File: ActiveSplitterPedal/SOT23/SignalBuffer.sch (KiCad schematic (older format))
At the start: 11 parts, among them SW1 SW_SPDT, U1 OPA842, U5 DG468DV_T1_E3

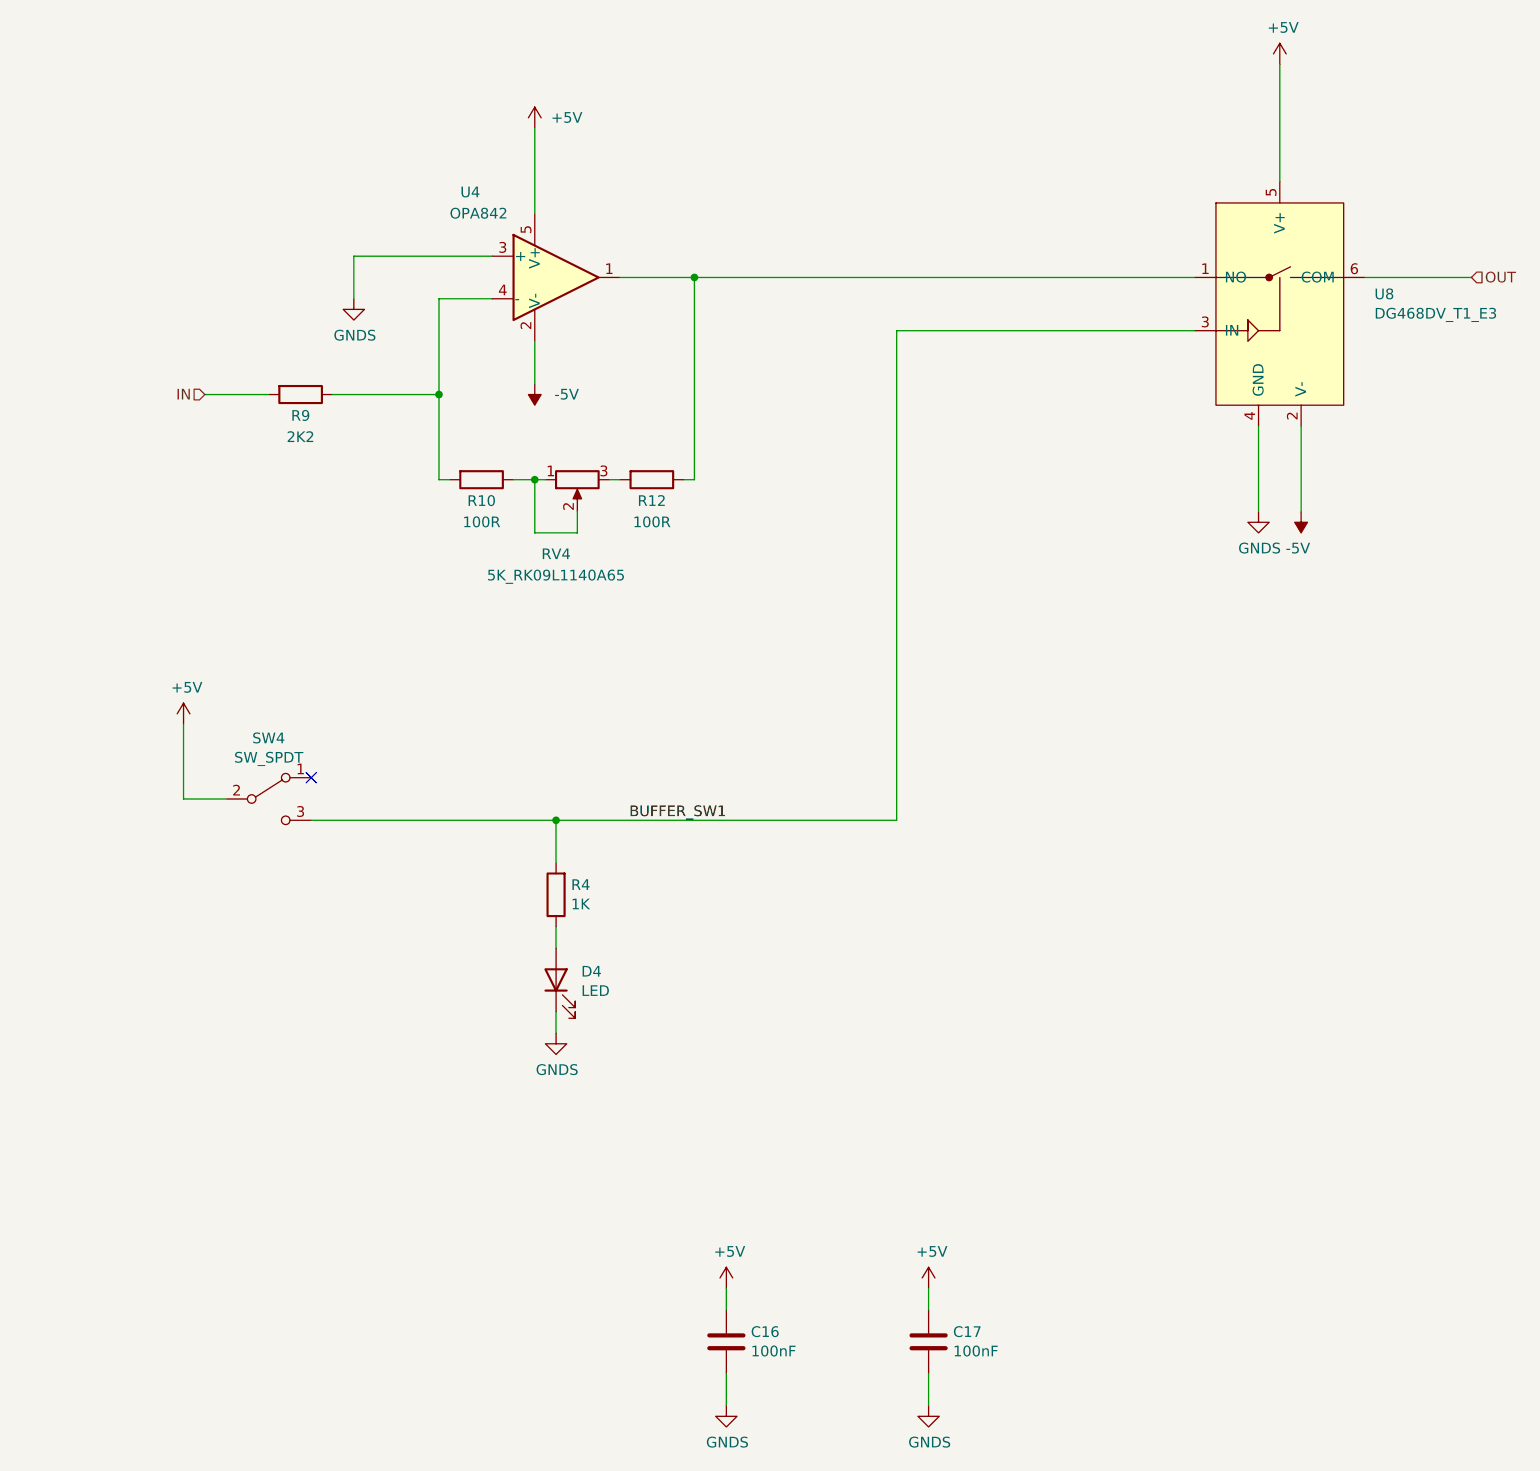
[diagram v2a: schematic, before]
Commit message: upgraded opamp from OPA842 to OPA197 (better performance/lower price)
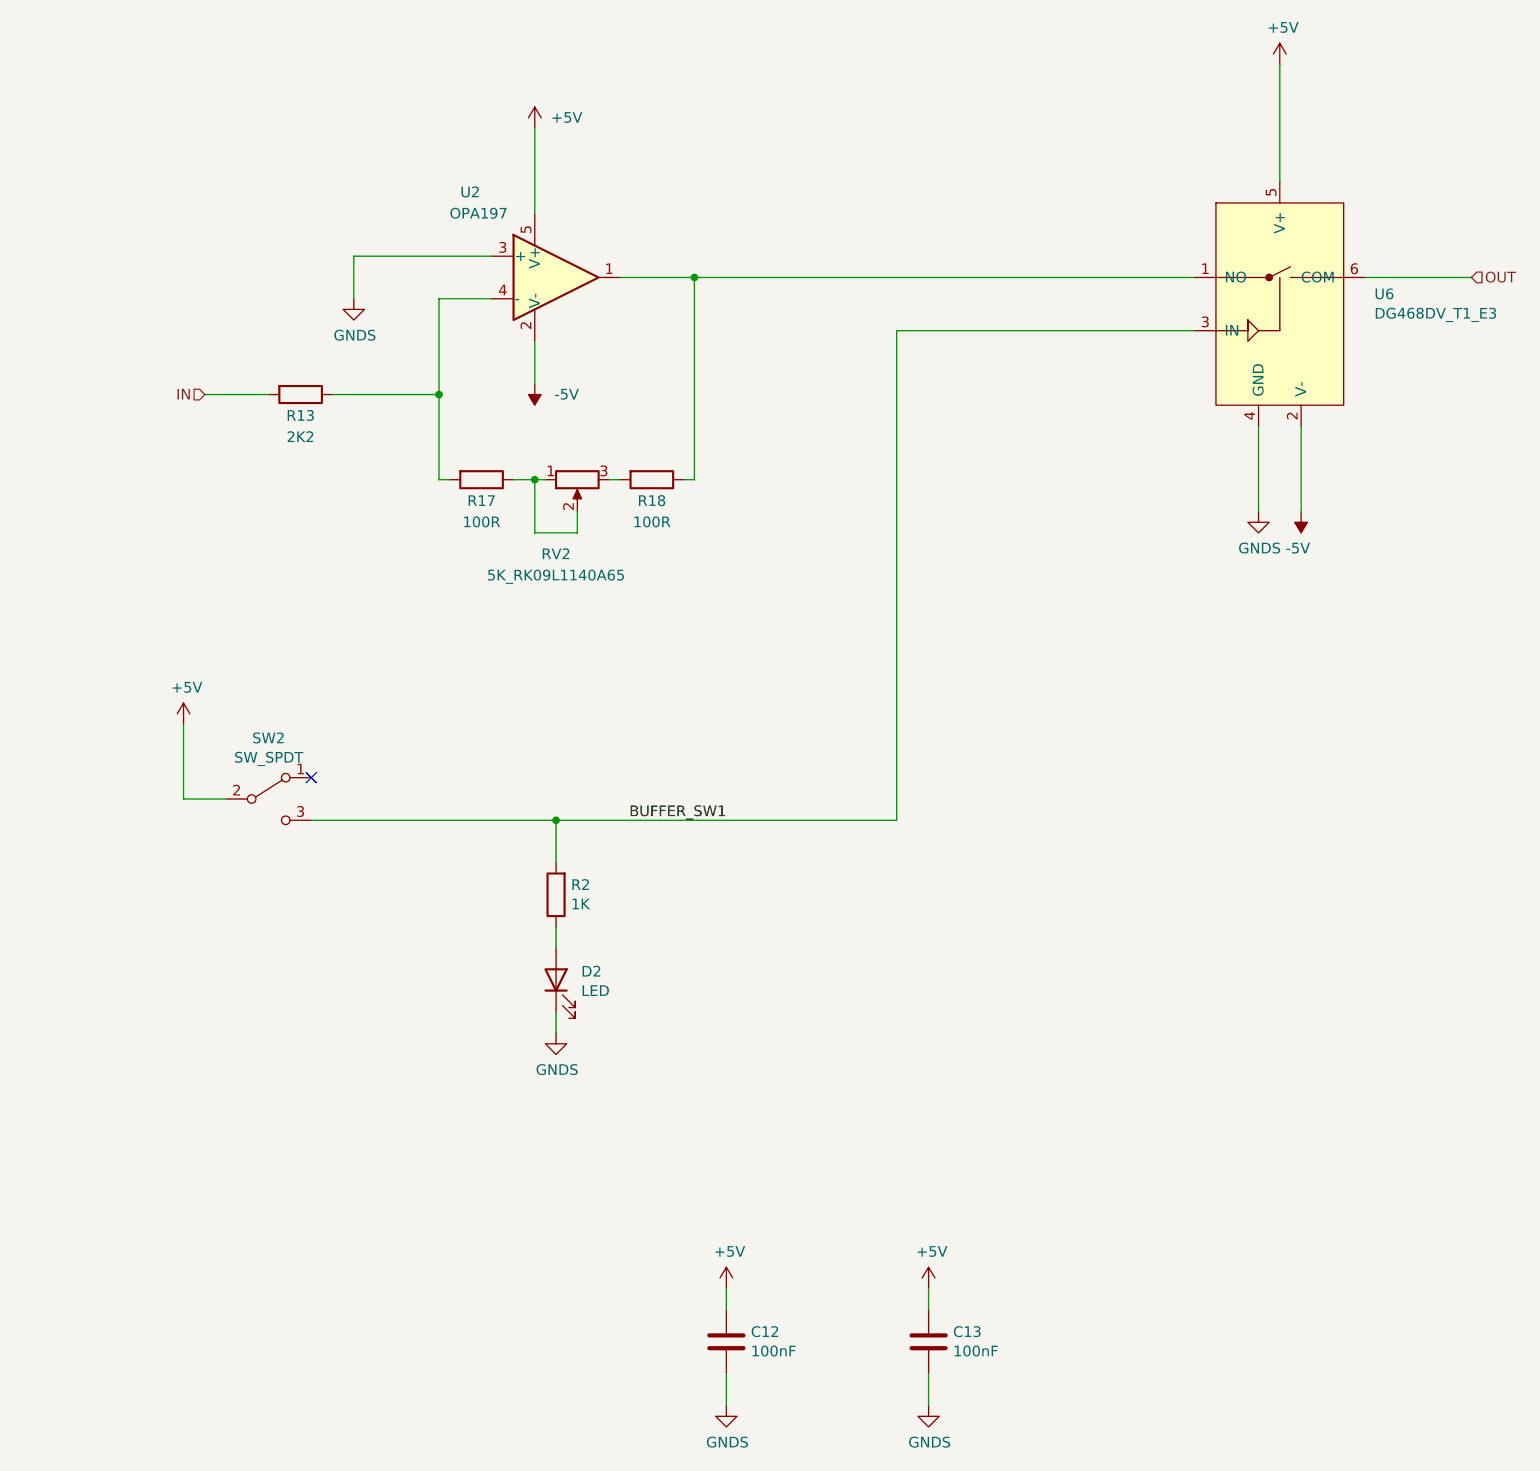
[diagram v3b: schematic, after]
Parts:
- U1: value OPA842 -> OPA197
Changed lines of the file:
@@
 $Descr A4 11693 8268
 encoding utf-8
-Sheet 3 6
+Sheet 5 6
 Title ""
 Date ""
@@
 AR Path="/5F365961/5F361F40" Ref="#PWR020"  Part="1"
 AR Path="/5F365B82/5F361F40" Ref="#PWR022"  Part="1"
-F 0 "#PWR022" H 4150 1250 50  0001 C CNN
+F 0 "#PWR018" H 4150 1250 50  0001 C CNN
 F 1 "+5V" H 4300 1450 50  0000 C CNN
 F 2 "" H 4150 1400 50  0001 C CNN
@@
 AR Path="/5F365961/5F3E136B" Ref="#PWR0113"  Part="1"
 AR Path="/5F365B82/5F3E136B" Ref="#PWR0119"  Part="1"
-F 0 "#PWR0119" H 7650 950 50  0001 C CNN
+F 0 "#PWR0107" H 7650 950 50  0001 C CNN
 F 1 "+5V" H 7665 1273 50  0000 C CNN
 F 2 "" H 7650 1100 50  0001 C CNN
@@
 AR Path="/5F365961/5F3E2841" Ref="#PWR0114"  Part="1"
 AR Path="/5F365B82/5F3E2841" Ref="#PWR0120"  Part="1"
-F 0 "#PWR0120" H 7750 3300 50  0001 C CNN
+F 0 "#PWR0108" H 7750 3300 50  0001 C CNN
 F 1 "-5V" H 7765 3373 50  0000 C CNN
 F 2 "" H 7750 3200 50  0001 C CNN
@@
 AR Path="/5F365961/5F3E3339" Ref="#PWR0116"  Part="1"
 AR Path="/5F365B82/5F3E3339" Ref="#PWR0122"  Part="1"
-F 0 "#PWR0122" H 6000 6700 50  0001 C CNN
+F 0 "#PWR0110" H 6000 6700 50  0001 C CNN
 F 1 "+5V" H 6015 7023 50  0000 C CNN
 F 2 "" H 6000 6850 50  0001 C CNN
@@
 AR Path="/5F365961/5F3E352F" Ref="C15"  Part="1"
 AR Path="/5F365B82/5F3E352F" Ref="C17"  Part="1"
-F 0 "C17" H 6115 7146 50  0000 L CNN
+F 0 "C13" H 6115 7146 50  0000 L CNN
 F 1 "100nF" H 6115 7055 50  0000 L CNN
 F 2 "Capacitor_SMD:C_0805_2012Metric_Pad1.15x1.40mm_HandSolder" H 6038 6950 50  0001 C CNN
@@
 AR Path="/5F365961/5F3E4DA7" Ref="#PWR0118"  Part="1"
 AR Path="/5F365B82/5F3E4DA7" Ref="#PWR0124"  Part="1"
-F 0 "#PWR0124" H 5050 6700 50  0001 C CNN
+F 0 "#PWR0112" H 5050 6700 50  0001 C CNN
 F 1 "+5V" H 5065 7023 50  0000 C CNN
 F 2 "" H 5050 6850 50  0001 C CNN
@@
 AR Path="/5F365961/5F3E4DAE" Ref="C14"  Part="1"
 AR Path="/5F365B82/5F3E4DAE" Ref="C16"  Part="1"
-F 0 "C16" H 5165 7146 50  0000 L CNN
+F 0 "C12" H 5165 7146 50  0000 L CNN
 F 1 "100nF" H 5165 7055 50  0000 L CNN
 F 2 "Capacitor_SMD:C_0805_2012Metric_Pad1.15x1.40mm_HandSolder" H 5088 6950 50  0001 C CNN
@@
 AR Path="/5F365961/5F34D1A6" Ref="U7"  Part="1"
 AR Path="/5F365B82/5F34D1A6" Ref="U8"  Part="1"
-F 0 "U8" H 8094 2221 50  0000 L CNN
+F 0 "U6" H 8094 2221 50  0000 L CNN
 F 1 "DG468DV_T1_E3" H 8094 2130 50  0000 L CNN
 F 2 "Package_SO:TSOP-6_1.65x3.05mm_P0.95mm" H 7650 2250 50  0001 C CNN
@@
 AR Path="/5F365961/5F35037B" Ref="#PWR040"  Part="1"
 AR Path="/5F365B82/5F35037B" Ref="#PWR043"  Part="1"
-F 0 "#PWR043" H 7550 2950 50  0001 C CNN
+F 0 "#PWR037" H 7550 2950 50  0001 C CNN
 F 1 "GNDS" H 7555 3027 50  0000 C CNN
 F 2 "" H 7550 3200 50  0001 C CNN
@@
 AR Path="/5F365961/5F350C0B" Ref="#PWR039"  Part="1"
 AR Path="/5F365B82/5F350C0B" Ref="#PWR042"  Part="1"
-F 0 "#PWR042" H 6000 7150 50  0001 C CNN
+F 0 "#PWR036" H 6000 7150 50  0001 C CNN
 F 1 "GNDS" H 6005 7227 50  0000 C CNN
 F 2 "" H 6000 7400 50  0001 C CNN
@@
 AR Path="/5F365961/5F350E14" Ref="#PWR038"  Part="1"
 AR Path="/5F365B82/5F350E14" Ref="#PWR041"  Part="1"
-F 0 "#PWR041" H 5050 7150 50  0001 C CNN
+F 0 "#PWR035" H 5050 7150 50  0001 C CNN
 F 1 "GNDS" H 5055 7227 50  0000 C CNN
 F 2 "" H 5050 7400 50  0001 C CNN
@@
 AR Path="/5F365961/5F361BF5" Ref="#PWR021"  Part="1"
 AR Path="/5F365B82/5F361BF5" Ref="#PWR023"  Part="1"
-F 0 "#PWR023" H 4150 2700 50  0001 C CNN
+F 0 "#PWR019" H 4150 2700 50  0001 C CNN
 F 1 "-5V" H 4000 2650 50  0000 C CNN
 F 2 "" H 4150 2600 50  0001 C CNN
@@
 AR Path="/5F365961/5F35E576" Ref="U3"  Part="1"
 AR Path="/5F365B82/5F35E576" Ref="U4"  Part="1"
-F 0 "U4" H 3800 2500 50  0000 L CNN
-F 1 "OPA842" H 3750 2400 50  0000 L CNN
+F 0 "U2" H 3800 2500 50  0000 L CNN
+F 1 "OPA197" H 3750 2400 50  0000 L CNN
 F 2 "Package_TO_SOT_SMD:SOT-23-5" H 4150 1900 50  0001 L CNN
-F 3 "http://www.ti.com/lit/ds/symlink/opa842.pdf" H 4250 2300 50  0001 C CNN
+F 3 "https://www.ti.com/lit/ds/symlink/opa197.pdf" H 4250 2300 50  0001 C CNN
 	1    4250 2100
 	1    0    0    -1
@@
 AR Path="/5F365961/5F374B42" Ref="R11"  Part="1"
 AR Path="/5F3658F9/5F374B42" Ref="R13"  Part="1"
-F 0 "R9" V 3150 2650 50  0000 C CNN
+F 0 "R13" V 3150 2650 50  0000 C CNN
 F 1 "2K2" V 3250 2650 50  0000 C CNN
 F 2 "Resistor_SMD:R_0805_2012Metric_Pad1.15x1.40mm_HandSolder" V 2980 2650 50  0001 C CNN
@@
 AR Path="/5F365961/5F377EED" Ref="#PWR045"  Part="1"
 AR Path="/5F3658F9/5F377EED" Ref="#PWR046"  Part="1"
-F 0 "#PWR044" H 3300 1950 50  0001 C CNN
+F 0 "#PWR046" H 3300 1950 50  0001 C CNN
 F 1 "GNDS" H 3305 2027 50  0000 C CNN
 F 2 "" H 3300 2200 50  0001 C CNN
@@
 AR Path="/5F365961/5F37ADE4" Ref="RV3"  Part="1"
 AR Path="/5F3658F9/5F37ADE4" Ref="RV2"  Part="1"
-F 0 "RV4" V 4700 3150 50  0000 C CNN
+F 0 "RV2" V 4700 3150 50  0000 C CNN
 F 1 "5K_RK09L1140A65" V 4800 3150 50  0000 C CNN
 F 2 "Potentiometer_THT:Potentiometer_Alps_RK09L_Single_Vertical" H 4350 3050 50  0001 C CNN
@@
 AR Path="/5F365961/5F37F653" Ref="R14"  Part="1"
 AR Path="/5F3658F9/5F37F653" Ref="R17"  Part="1"
-F 0 "R10" V 4000 3050 50  0000 C CNN
+F 0 "R17" V 4000 3050 50  0000 C CNN
 F 1 "100R" V 4100 3050 50  0000 C CNN
 F 2 "Resistor_SMD:R_0805_2012Metric_Pad1.15x1.40mm_HandSolder" V 3830 3050 50  0001 C CNN
@@
 AR Path="/5F365961/5F37FC84" Ref="R16"  Part="1"
 AR Path="/5F3658F9/5F37FC84" Ref="R18"  Part="1"
-F 0 "R12" V 4800 3050 50  0000 C CNN
+F 0 "R18" V 4800 3050 50  0000 C CNN
 F 1 "100R" V 4900 3050 50  0000 C CNN
 F 2 "Resistor_SMD:R_0805_2012Metric_Pad1.15x1.40mm_HandSolder" V 4630 3050 50  0001 C CNN
@@
 AR Path="/5F365B82/5F3D2157" Ref="#PWR0103"  Part="1"
 AR Path="/5F350192/5F3D2157" Ref="#PWR0121"  Part="1"
-F 0 "#PWR0103" H 2500 4050 50  0001 C CNN
+F 0 "#PWR0115" H 2500 4050 50  0001 C CNN
 F 1 "+5V" H 2515 4373 50  0000 C CNN
 F 2 "" H 2500 4200 50  0001 C CNN
@@
 AR Path="/5F365961/5F3D215D" Ref="R3"  Part="1"
 AR Path="/5F365B82/5F3D215D" Ref="R4"  Part="1"
-F 0 "R4" H 4180 4954 50  0000 R CNN
+F 0 "R2" H 4180 4954 50  0000 R CNN
 F 1 "1K" H 4180 5045 50  0000 R CNN
 F 2 "Resistor_SMD:R_0805_2012Metric_Pad1.15x1.40mm_HandSolder" V 4180 5000 50  0001 C CNN
@@
 AR Path="/5F365961/5F3D2166" Ref="D3"  Part="1"
 AR Path="/5F365B82/5F3D2166" Ref="D4"  Part="1"
-F 0 "D4" V 4289 5282 50  0000 R CNN
+F 0 "D2" V 4289 5282 50  0000 R CNN
 F 1 "LED" V 4198 5282 50  0000 R CNN
 F 2 "LED_THT:LED_D5.0mm" H 4250 5400 50  0001 C CNN
@@
 AR Path="/5F365B82/5F3D216E" Ref="#PWR0105"  Part="1"
 AR Path="/5F350192/5F3D216E" Ref="#PWR0123"  Part="1"
-F 0 "#PWR0105" H 4250 5400 50  0001 C CNN
+F 0 "#PWR0117" H 4250 5400 50  0001 C CNN
 F 1 "GNDS" H 4255 5477 50  0000 C CNN
 F 2 "" H 4250 5650 50  0001 C CNN
@@
 AR Path="/5F365961/5F3D2176" Ref="SW3"  Part="1"
 AR Path="/5F365B82/5F3D2176" Ref="SW4"  Part="1"
-F 0 "SW4" H 2900 4835 50  0000 C CNN
+F 0 "SW2" H 2900 4835 50  0000 C CNN
 F 1 "SW_SPDT" H 2900 4744 50  0000 C CNN
 F 2 "RS_Switches:SPDT_Slide_Switch_Latching_Vertical_THT_8x9.3mm_734-7303" H 2900 4550 50  0001 C CNN

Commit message: Completed RevA layout
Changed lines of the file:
@@
 $Descr A4 11693 8268
 encoding utf-8
-Sheet 5 6
+Sheet 6 7
 Title ""
 Date ""
@@
 AR Path="/5F365961/5F361F40" Ref="#PWR020"  Part="1"
 AR Path="/5F365B82/5F361F40" Ref="#PWR022"  Part="1"
-F 0 "#PWR018" H 4150 1250 50  0001 C CNN
+F 0 "#PWR016" H 4150 1250 50  0001 C CNN
 F 1 "+5V" H 4300 1450 50  0000 C CNN
 F 2 "" H 4150 1400 50  0001 C CNN
@@
 AR Path="/5F365961/5F3E136B" Ref="#PWR0113"  Part="1"
 AR Path="/5F365B82/5F3E136B" Ref="#PWR0119"  Part="1"
-F 0 "#PWR0107" H 7650 950 50  0001 C CNN
+F 0 "#PWR0101" H 7650 950 50  0001 C CNN
 F 1 "+5V" H 7665 1273 50  0000 C CNN
 F 2 "" H 7650 1100 50  0001 C CNN
@@
 AR Path="/5F365961/5F3E2841" Ref="#PWR0114"  Part="1"
 AR Path="/5F365B82/5F3E2841" Ref="#PWR0120"  Part="1"
-F 0 "#PWR0108" H 7750 3300 50  0001 C CNN
+F 0 "#PWR0102" H 7750 3300 50  0001 C CNN
 F 1 "-5V" H 7765 3373 50  0000 C CNN
 F 2 "" H 7750 3200 50  0001 C CNN
@@
 AR Path="/5F365961/5F3E3339" Ref="#PWR0116"  Part="1"
 AR Path="/5F365B82/5F3E3339" Ref="#PWR0122"  Part="1"
-F 0 "#PWR0110" H 6000 6700 50  0001 C CNN
+F 0 "#PWR0104" H 6000 6700 50  0001 C CNN
 F 1 "+5V" H 6015 7023 50  0000 C CNN
 F 2 "" H 6000 6850 50  0001 C CNN
@@
 AR Path="/5F365961/5F3E352F" Ref="C15"  Part="1"
 AR Path="/5F365B82/5F3E352F" Ref="C17"  Part="1"
-F 0 "C13" H 6115 7146 50  0000 L CNN
+F 0 "C7" H 6115 7146 50  0000 L CNN
 F 1 "100nF" H 6115 7055 50  0000 L CNN
 F 2 "Capacitor_SMD:C_0805_2012Metric_Pad1.15x1.40mm_HandSolder" H 6038 6950 50  0001 C CNN
@@
 AR Path="/5F365961/5F3E4DA7" Ref="#PWR0118"  Part="1"
 AR Path="/5F365B82/5F3E4DA7" Ref="#PWR0124"  Part="1"
-F 0 "#PWR0112" H 5050 6700 50  0001 C CNN
+F 0 "#PWR0106" H 5050 6700 50  0001 C CNN
 F 1 "+5V" H 5065 7023 50  0000 C CNN
 F 2 "" H 5050 6850 50  0001 C CNN
@@
 AR Path="/5F365961/5F3E4DAE" Ref="C14"  Part="1"
 AR Path="/5F365B82/5F3E4DAE" Ref="C16"  Part="1"
-F 0 "C12" H 5165 7146 50  0000 L CNN
+F 0 "C4" H 5165 7146 50  0000 L CNN
 F 1 "100nF" H 5165 7055 50  0000 L CNN
 F 2 "Capacitor_SMD:C_0805_2012Metric_Pad1.15x1.40mm_HandSolder" H 5088 6950 50  0001 C CNN
@@
 AR Path="/5F365961/5F34D1A6" Ref="U7"  Part="1"
 AR Path="/5F365B82/5F34D1A6" Ref="U8"  Part="1"
-F 0 "U6" H 8094 2221 50  0000 L CNN
+F 0 "U5" H 8094 2221 50  0000 L CNN
 F 1 "DG468DV_T1_E3" H 8094 2130 50  0000 L CNN
 F 2 "Package_SO:TSOP-6_1.65x3.05mm_P0.95mm" H 7650 2250 50  0001 C CNN
@@
 AR Path="/5F365961/5F35037B" Ref="#PWR040"  Part="1"
 AR Path="/5F365B82/5F35037B" Ref="#PWR043"  Part="1"
-F 0 "#PWR037" H 7550 2950 50  0001 C CNN
+F 0 "#PWR034" H 7550 2950 50  0001 C CNN
 F 1 "GNDS" H 7555 3027 50  0000 C CNN
 F 2 "" H 7550 3200 50  0001 C CNN
@@
 AR Path="/5F365961/5F350C0B" Ref="#PWR039"  Part="1"
 AR Path="/5F365B82/5F350C0B" Ref="#PWR042"  Part="1"
-F 0 "#PWR036" H 6000 7150 50  0001 C CNN
+F 0 "#PWR029" H 6000 7150 50  0001 C CNN
 F 1 "GNDS" H 6005 7227 50  0000 C CNN
 F 2 "" H 6000 7400 50  0001 C CNN
@@
 AR Path="/5F365961/5F350E14" Ref="#PWR038"  Part="1"
 AR Path="/5F365B82/5F350E14" Ref="#PWR041"  Part="1"
-F 0 "#PWR035" H 5050 7150 50  0001 C CNN
+F 0 "#PWR027" H 5050 7150 50  0001 C CNN
 F 1 "GNDS" H 5055 7227 50  0000 C CNN
 F 2 "" H 5050 7400 50  0001 C CNN
@@
 AR Path="/5F365961/5F361BF5" Ref="#PWR021"  Part="1"
 AR Path="/5F365B82/5F361BF5" Ref="#PWR023"  Part="1"
-F 0 "#PWR019" H 4150 2700 50  0001 C CNN
+F 0 "#PWR017" H 4150 2700 50  0001 C CNN
 F 1 "-5V" H 4000 2650 50  0000 C CNN
 F 2 "" H 4150 2600 50  0001 C CNN
@@
 AR Path="/5F365961/5F35E576" Ref="U3"  Part="1"
 AR Path="/5F365B82/5F35E576" Ref="U4"  Part="1"
-F 0 "U2" H 3800 2500 50  0000 L CNN
+F 0 "U1" H 3800 2500 50  0000 L CNN
 F 1 "OPA197" H 3750 2400 50  0000 L CNN
 F 2 "Package_TO_SOT_SMD:SOT-23-5" H 4150 1900 50  0001 L CNN
@@
 AR Path="/5F365961/5F374B42" Ref="R11"  Part="1"
 AR Path="/5F3658F9/5F374B42" Ref="R13"  Part="1"
-F 0 "R13" V 3150 2650 50  0000 C CNN
+F 0 "R15" V 3150 2650 50  0000 C CNN
 F 1 "2K2" V 3250 2650 50  0000 C CNN
 F 2 "Resistor_SMD:R_0805_2012Metric_Pad1.15x1.40mm_HandSolder" V 2980 2650 50  0001 C CNN
@@
 AR Path="/5F365961/5F377EED" Ref="#PWR045"  Part="1"
 AR Path="/5F3658F9/5F377EED" Ref="#PWR046"  Part="1"
-F 0 "#PWR046" H 3300 1950 50  0001 C CNN
+F 0 "#PWR047" H 3300 1950 50  0001 C CNN
 F 1 "GNDS" H 3305 2027 50  0000 C CNN
 F 2 "" H 3300 2200 50  0001 C CNN
@@
 AR Path="/5F365961/5F37ADE4" Ref="RV3"  Part="1"
 AR Path="/5F3658F9/5F37ADE4" Ref="RV2"  Part="1"
-F 0 "RV2" V 4700 3150 50  0000 C CNN
+F 0 "RV1" V 4700 3150 50  0000 C CNN
 F 1 "5K_RK09L1140A65" V 4800 3150 50  0000 C CNN
 F 2 "Potentiometer_THT:Potentiometer_Alps_RK09L_Single_Vertical" H 4350 3050 50  0001 C CNN
@@
 AR Path="/5F365961/5F37F653" Ref="R14"  Part="1"
 AR Path="/5F3658F9/5F37F653" Ref="R17"  Part="1"
-F 0 "R17" V 4000 3050 50  0000 C CNN
+F 0 "R19" V 4000 3050 50  0000 C CNN
 F 1 "100R" V 4100 3050 50  0000 C CNN
 F 2 "Resistor_SMD:R_0805_2012Metric_Pad1.15x1.40mm_HandSolder" V 3830 3050 50  0001 C CNN
@@
 AR Path="/5F365961/5F37FC84" Ref="R16"  Part="1"
 AR Path="/5F3658F9/5F37FC84" Ref="R18"  Part="1"
-F 0 "R18" V 4800 3050 50  0000 C CNN
+F 0 "R20" V 4800 3050 50  0000 C CNN
 F 1 "100R" V 4900 3050 50  0000 C CNN
 F 2 "Resistor_SMD:R_0805_2012Metric_Pad1.15x1.40mm_HandSolder" V 4630 3050 50  0001 C CNN
@@
 AR Path="/5F365B82/5F3D2157" Ref="#PWR0103"  Part="1"
 AR Path="/5F350192/5F3D2157" Ref="#PWR0121"  Part="1"
-F 0 "#PWR0115" H 2500 4050 50  0001 C CNN
+F 0 "#PWR0121" H 2500 4050 50  0001 C CNN
 F 1 "+5V" H 2515 4373 50  0000 C CNN
 F 2 "" H 2500 4200 50  0001 C CNN
@@
 AR Path="/5F365961/5F3D215D" Ref="R3"  Part="1"
 AR Path="/5F365B82/5F3D215D" Ref="R4"  Part="1"
-F 0 "R2" H 4180 4954 50  0000 R CNN
+F 0 "R1" H 4180 4954 50  0000 R CNN
 F 1 "1K" H 4180 5045 50  0000 R CNN
 F 2 "Resistor_SMD:R_0805_2012Metric_Pad1.15x1.40mm_HandSolder" V 4180 5000 50  0001 C CNN
@@
 AR Path="/5F365961/5F3D2166" Ref="D3"  Part="1"
 AR Path="/5F365B82/5F3D2166" Ref="D4"  Part="1"
-F 0 "D2" V 4289 5282 50  0000 R CNN
+F 0 "D1" V 4289 5282 50  0000 R CNN
 F 1 "LED" V 4198 5282 50  0000 R CNN
 F 2 "LED_THT:LED_D5.0mm" H 4250 5400 50  0001 C CNN
@@
 AR Path="/5F365B82/5F3D216E" Ref="#PWR0105"  Part="1"
 AR Path="/5F350192/5F3D216E" Ref="#PWR0123"  Part="1"
-F 0 "#PWR0117" H 4250 5400 50  0001 C CNN
+F 0 "#PWR0123" H 4250 5400 50  0001 C CNN
 F 1 "GNDS" H 4255 5477 50  0000 C CNN
 F 2 "" H 4250 5650 50  0001 C CNN
@@
 AR Path="/5F365961/5F3D2176" Ref="SW3"  Part="1"
 AR Path="/5F365B82/5F3D2176" Ref="SW4"  Part="1"
-F 0 "SW2" H 2900 4835 50  0000 C CNN
+F 0 "SW1" H 2900 4835 50  0000 C CNN
 F 1 "SW_SPDT" H 2900 4744 50  0000 C CNN
 F 2 "RS_Switches:SPDT_Slide_Switch_Latching_Vertical_THT_8x9.3mm_734-7303" H 2900 4550 50  0001 C CNN
